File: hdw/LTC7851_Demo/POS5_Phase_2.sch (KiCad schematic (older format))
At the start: 0 parts

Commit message: Duplicated master phase, added status LEDs and a few test points
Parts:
- added C? (x2): 1uF, symbol Custom_Library:C_Custom
- added C? (x2): 0.1uF, symbol Custom_Library:C_Custom
- added C?: 0.22uF, symbol Custom_Library:C_Custom
- added C? (x2): 22uF, symbol Custom_Library:C_Custom
- added C? (x2): 100uF, symbol Custom_Library:C_Custom
- added C? (x6): 100uF, symbol Custom_Library:CP_Tant_Custom
- added L?: 0.47uH, symbol Custom_Library:L_Custom
- added R? (x2): 2, symbol Custom_Library:R_Custom
- added R?: 1.4k, symbol Custom_Library:R_Custom
- added TP? (x2): TP, symbol Custom_Library:TP
- added U?: SiC779, symbol Custom_Library:SiC779
- added U?: LTC7851UHH, symbol Custom_Library:LTC7851UHH
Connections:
- net labels added: +12V, +5.5V_MNG, +5V, GND, POS5_COMP, POS5_EXTVCC, POS5_IAVG, POS5_ILIM, POS5_ISNS1_+, POS5_ISNS1_-, POS5_PGOOD_OC, POS5_RUN, POS5_SMOD, POS5_SS, POS5_VOSNS, ~POS5_THDN
- wire segments 0 -> 110
- no-connect marks 0 -> 2
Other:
- note added: "Remove bulk caps from onsheet when bringing into project"
- note added: "Route as diff pair"

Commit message: Assigned some custom footprints
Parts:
- U?: footprint (none) -> Custom Footprints Library:MLP66-40_6x6mm_Pitch0.5mm
- U?: footprint (none) -> Custom Footprints Library:QFN-58-1EP_9x5mm_Pitch0.4mm
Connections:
- net labels added: POS5_ISNS2_+, POS5_ISNS2_-
- net labels removed: POS5_ISNS1_+, POS5_ISNS1_-
- wire segments 110 -> 112
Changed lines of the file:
@@
 F 0 "U?" H 6080 960 50  0000 C CNN
 F 1 "SiC779" H 6080 4660 50  0000 C CNN
-F 2 "" H 4430 3560 50  0001 C CNN
+F 2 "Custom Footprints Library:MLP66-40_6x6mm_Pitch0.5mm" H 4430 3560 50  0001 C CNN
 F 3 "http://www.vishay.com/docs/67538/sic779.pdf" H 6080 2810 50  0001 C CNN
 F 4 "SIC779CD-T1-GE3CT-ND" H 6080 2810 50  0001 C CNN "Digi-Key PN"
@@
 F 0 "U?" H 2910 2160 50  0000 R CNN
 F 1 "LTC7851UHH" H 2510 6260 50  0000 C CNN
-F 2 "" H -140 4910 50  0001 C CNN
+F 2 "Custom Footprints Library:QFN-58-1EP_9x5mm_Pitch0.4mm" H -140 4910 50  0001 C CNN
 F 3 "http://www.analog.com/media/en/technical-documentation/data-sheets/LTC7851.pdf" H 2510 4210 50  0001 C CNN
 F 4 "LTC7851IUHH#PBF-ND" H 2510 4210 50  0001 C CNN "Digi-Key PN"
@@
 POS5_RUN
 Text Label 3160 3310 0    50   ~ 0
-POS5_ISNS1_+
+POS5_ISNS2_+
 Text Label 3160 3410 0    50   ~ 0
-POS5_ISNS1_-
+POS5_ISNS2_-
 Text Notes 3270 3670 0    50   ~ 0
 Route as diff pair
@@
 Text GLabel 3060 5110 2    50   UnSpc ~ 0
 POS5_EXTVCC
+Wire Wire Line
+	6730 4110 6810 4110
+Wire Wire Line
+	6810 4110 6810 4010
+Connection ~ 6810 4010
 $EndSCHEMATC

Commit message: Annotated schematic
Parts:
- gave numbers to parts that had none: 23

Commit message: Added Digi-Key part numbers for all parts
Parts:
- C504, C509: Digi-Key PN PN -> 1276-6524-1-ND
- C506, C508: Digi-Key PN PN -> 490-4779-1-ND
- C510: Digi-Key PN PN -> 490-5402-1-ND
- C512: Digi-Key PN PN -> 587-3432-1-ND
- R501, R502: Digi-Key PN PN -> RMCF0603FT2R00CT-ND
- R503: Digi-Key PN PN -> P1.40KHCT-ND
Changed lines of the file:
@@
 F 5 "16V" H 4410 1340 50  0000 R CNN "Voltage"
 F 6 "X7R" H 4410 1240 50  0000 R CNN "Dielectric"
-F 7 "PN" H 4985 1840 60  0001 C CNN "Digi-Key PN"
+F 7 "1276-6524-1-ND" H 4985 1840 60  0001 C CNN "Digi-Key PN"
 	1    4560 1340
 	1    0    0    -1
@@
 F 2 "" H 6980 2470 50  0001 C CNN
 F 3 "" H 6980 2470 50  0001 C CNN
-F 4 "PN" H 7280 2870 60  0001 C CNN "Digi-Key PN"
+F 4 "RMCF0603FT2R00CT-ND" H 7280 2870 60  0001 C CNN "Digi-Key PN"
 F 5 "0603" H 7080 2550 50  0000 L CNN "display_footprint"
 F 6 "1%" H 7080 2470 50  0000 L CNN "Tolerance"
@@
 F 5 "50V" H 6830 2850 50  0000 R CNN "Voltage"
 F 6 "X7R" H 6830 2750 50  0000 R CNN "Dielectric"
-F 7 "PN" H 7405 3350 60  0001 C CNN "Digi-Key PN"
+F 7 "490-4779-1-ND" H 7405 3350 60  0001 C CNN "Digi-Key PN"
 	1    6980 2850
 	1    0    0    -1
@@
 F 2 "" H 7190 3770 50  0001 C CNN
 F 3 "" H 7190 3770 50  0001 C CNN
-F 4 "PN" H 7490 4170 60  0001 C CNN "Digi-Key PN"
+F 4 "P1.40KHCT-ND" H 7490 4170 60  0001 C CNN "Digi-Key PN"
 F 5 "0603" H 7290 3850 50  0000 L CNN "display_footprint"
 F 6 "1%" H 7290 3770 50  0000 L CNN "Tolerance"
@@
 F 2 "" H 7478 3890 50  0001 C CNN
 F 3 "" H 7465 4140 50  0001 C CNN
-F 4 "PN" H 7865 4540 60  0001 C CNN "Digi-Key PN"
+F 4 "490-5402-1-ND" H 7865 4540 60  0001 C CNN "Digi-Key PN"
 F 5 "0603" V 7098 4040 50  0000 C CNN "display_footprint"
 F 6 "50V" V 7189 4040 50  0000 C CNN "Voltage"
@@
 F 5 "10V" H 8270 3540 50  0000 R CNN "Voltage"
 F 6 "X5R" H 8270 3440 50  0000 R CNN "Dielectric"
-F 7 "PN" H 8845 4040 60  0001 C CNN "Digi-Key PN"
+F 7 "587-3432-1-ND" H 8845 4040 60  0001 C CNN "Digi-Key PN"
 	1    8420 3540
 	1    0    0    -1
@@
 F 5 "50V" H 5030 1870 50  0000 R CNN "Voltage"
 F 6 "X7R" H 5030 1770 50  0000 R CNN "Dielectric"
-F 7 "PN" H 5605 2370 60  0001 C CNN "Digi-Key PN"
+F 7 "490-4779-1-ND" H 5605 2370 60  0001 C CNN "Digi-Key PN"
 	1    5180 1870
 	1    0    0    -1
@@
 F 2 "" H 5180 1340 50  0001 C CNN
 F 3 "" H 5180 1340 50  0001 C CNN
-F 4 "PN" H 5480 1740 60  0001 C CNN "Digi-Key PN"
+F 4 "RMCF0603FT2R00CT-ND" H 5480 1740 60  0001 C CNN "Digi-Key PN"
 F 5 "0603" H 5280 1420 50  0000 L CNN "display_footprint"
 F 6 "1%" H 5280 1340 50  0000 L CNN "Tolerance"
@@
 F 5 "16V" H 7130 1340 50  0000 R CNN "Voltage"
 F 6 "X7R" H 7130 1240 50  0000 R CNN "Dielectric"
-F 7 "PN" H 7705 1840 60  0001 C CNN "Digi-Key PN"
+F 7 "1276-6524-1-ND" H 7705 1840 60  0001 C CNN "Digi-Key PN"
 	1    7280 1340
 	1    0    0    -1

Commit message: Assigned footprints
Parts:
- C501, C502, C503, C505, C507, C515: footprint (none) -> Capacitors_Tantalum_SMD:CP_Tantalum_Case-B_EIA-3528-21_Reflow
- C504: footprint (none) -> Capacitors_SMD:C_0603_HandSoldering
- C506, C508, C509, C510: footprint (none) -> Capacitors_SMD:C_0603
- C511, C512, C513, C514: footprint (none) -> Capacitors_SMD:C_1210
- L501: footprint (none) -> Inductors_SMD:L_Vishay_IHLP-4040
- R501, R502, R503: footprint (none) -> Resistors_SMD:R_0603
- TP501, TP502: footprint (none) -> Measurement_Points:Measurement_Point_Round-SMD-Pad_Small
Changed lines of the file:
@@
 F 0 "C504" H 4585 1440 50  0000 L CNN
 F 1 "1uF" H 4585 1240 50  0000 L CNN
-F 2 "" H 4598 1190 50  0001 C CNN
+F 2 "Capacitors_SMD:C_0603_HandSoldering" H 4598 1190 50  0001 C CNN
 F 3 "" H 4585 1440 50  0001 C CNN
 F 4 "0603" H 4410 1440 50  0000 R CNN "display_footprint"
@@
 F 0 "TP501" V 5430 2960 50  0000 L CNN
 F 1 "TP" H 5430 2960 50  0001 C CNN
-F 2 "" H 5430 2810 60  0000 C CNN
+F 2 "Measurement_Points:Measurement_Point_Round-SMD-Pad_Small" H 5430 2810 60  0001 C CNN
 F 3 "" H 5430 2810 60  0000 C CNN
 	1    5430 2810
@@
 F 0 "TP502" V 5430 3060 50  0000 L CNN
 F 1 "TP" H 5430 3060 50  0001 C CNN
-F 2 "" H 5430 2910 60  0000 C CNN
+F 2 "Measurement_Points:Measurement_Point_Round-SMD-Pad_Small" H 5430 2910 60  0001 C CNN
 F 3 "" H 5430 2910 60  0000 C CNN
 	1    5430 2910
@@
 F 0 "L501" V 7390 3310 50  0000 C CNN
 F 1 "0.47uH" V 7515 3310 50  0000 C CNN
-F 2 "" H 7440 3310 50  0001 C CNN
+F 2 "Inductors_SMD:L_Vishay_IHLP-4040" H 7440 3310 50  0001 C CNN
 F 3 "" H 7440 3310 50  0001 C CNN
 F 4 "541-2595-1-ND" H 7440 3310 50  0001 C CNN "Digi-Key PN"
@@
 F 0 "R502" H 6880 2470 50  0000 R CNN
 F 1 "2" V 6980 2470 50  0000 C CNN
-F 2 "" H 6980 2470 50  0001 C CNN
+F 2 "Resistors_SMD:R_0603" H 6980 2470 50  0001 C CNN
 F 3 "" H 6980 2470 50  0001 C CNN
 F 4 "RMCF0603FT2R00CT-ND" H 7280 2870 60  0001 C CNN "Digi-Key PN"
@@
 F 0 "C508" H 7005 2950 50  0000 L CNN
 F 1 "0.1uF" H 7005 2750 50  0000 L CNN
-F 2 "" H 7018 2700 50  0001 C CNN
+F 2 "Capacitors_SMD:C_0603" H 7018 2700 50  0001 C CNN
 F 3 "" H 7005 2950 50  0001 C CNN
 F 4 "0603" H 6830 2950 50  0000 R CNN "display_footprint"
@@
 F 0 "R503" H 7290 3920 50  0000 L CNN
 F 1 "1.4k" V 7190 3770 40  0000 C CNN
-F 2 "" H 7190 3770 50  0001 C CNN
+F 2 "Resistors_SMD:R_0603" H 7190 3770 50  0001 C CNN
 F 3 "" H 7190 3770 50  0001 C CNN
 F 4 "P1.40KHCT-ND" H 7490 4170 60  0001 C CNN "Digi-Key PN"
@@
 F 0 "C510" V 6916 4040 50  0000 C CNN
 F 1 "0.22uF" V 7007 3910 50  0000 L CNN
-F 2 "" H 7478 3890 50  0001 C CNN
+F 2 "Capacitors_SMD:C_0603" H 7478 3890 50  0001 C CNN
 F 3 "" H 7465 4140 50  0001 C CNN
 F 4 "490-5402-1-ND" H 7865 4540 60  0001 C CNN "Digi-Key PN"
@@
 F 0 "C511" H 7905 1440 50  0000 L CNN
 F 1 "22uF" H 7905 1240 50  0000 L CNN
-F 2 "" H 7918 1190 50  0001 C CNN
+F 2 "Capacitors_SMD:C_1210" H 7918 1190 50  0001 C CNN
 F 3 "" H 7905 1440 50  0001 C CNN
 F 4 "445-1436-1-ND" H 8305 1840 60  0001 C CNN "Digi-Key PN"
@@
 F 0 "C512" H 8445 3640 50  0000 L CNN
 F 1 "100uF" H 8445 3440 50  0000 L CNN
-F 2 "" H 8458 3390 50  0001 C CNN
+F 2 "Capacitors_SMD:C_1210" H 8458 3390 50  0001 C CNN
 F 3 "" H 8445 3640 50  0001 C CNN
 F 4 "1210" H 8270 3640 50  0000 R CNN "display_footprint"
@@
 F 0 "C506" H 5205 1970 50  0000 L CNN
 F 1 "0.1uF" H 5205 1770 50  0000 L CNN
-F 2 "" H 5218 1720 50  0001 C CNN
+F 2 "Capacitors_SMD:C_0603" H 5218 1720 50  0001 C CNN
 F 3 "" H 5205 1970 50  0001 C CNN
 F 4 "0603" H 5030 1970 50  0000 R CNN "display_footprint"
@@
 F 0 "R501" H 5080 1340 50  0000 R CNN
 F 1 "2" V 5180 1340 50  0000 C CNN
-F 2 "" H 5180 1340 50  0001 C CNN
+F 2 "Resistors_SMD:R_0603" H 5180 1340 50  0001 C CNN
 F 3 "" H 5180 1340 50  0001 C CNN
 F 4 "RMCF0603FT2R00CT-ND" H 5480 1740 60  0001 C CNN "Digi-Key PN"
@@
 F 0 "C509" H 7305 1440 50  0000 L CNN
 F 1 "1uF" H 7305 1240 50  0000 L CNN
-F 2 "" H 7318 1190 50  0001 C CNN
+F 2 "Capacitors_SMD:C_0603" H 7318 1190 50  0001 C CNN
 F 3 "" H 7305 1440 50  0001 C CNN
 F 4 "0603" H 7130 1440 50  0000 R CNN "display_footprint"
@@
 F 0 "C515" H 9645 3640 50  0000 L CNN
 F 1 "100uF" H 9645 3440 50  0000 L CNN
-F 2 "" H 9658 3390 50  0001 C CNN
+F 2 "Capacitors_Tantalum_SMD:CP_Tantalum_Case-B_EIA-3528-21_Reflow" H 9658 3390 50  0001 C CNN
 F 3 "" H 9645 3640 50  0001 C CNN
 F 4 "478-9994-1-ND" H 9620 3540 50  0001 C CNN "Digi-Key PN"
@@
 F 0 "C514" H 9045 3640 50  0000 L CNN
 F 1 "100uF" H 9045 3440 50  0000 L CNN
-F 2 "" H 9058 3390 50  0001 C CNN
+F 2 "Capacitors_SMD:C_1210" H 9058 3390 50  0001 C CNN
 F 3 "" H 9045 3640 50  0001 C CNN
 F 4 "587-3432-1-ND" H 9445 4040 60  0001 C CNN "Digi-Key PN"
@@
 F 0 "C513" H 8505 1440 50  0000 L CNN
 F 1 "22uF" H 8505 1240 50  0000 L CNN
-F 2 "" H 8518 1190 50  0001 C CNN
+F 2 "Capacitors_SMD:C_1210" H 8518 1190 50  0001 C CNN
 F 3 "" H 8505 1440 50  0001 C CNN
 F 4 "445-1436-1-ND" H 8905 1840 60  0001 C CNN "Digi-Key PN"
@@
 F 0 "C501" H 3355 7470 50  0000 L CNN
 F 1 "100uF" H 3355 7270 50  0000 L CNN
-F 2 "" H 3368 7220 50  0001 C CNN
+F 2 "Capacitors_Tantalum_SMD:CP_Tantalum_Case-B_EIA-3528-21_Reflow" H 3368 7220 50  0001 C CNN
 F 3 "" H 3355 7470 50  0001 C CNN
 F 4 "478-9994-1-ND" H 3330 7370 50  0001 C CNN "Digi-Key PN"
@@
 F 0 "C502" H 3955 7470 50  0000 L CNN
 F 1 "100uF" H 3955 7270 50  0000 L CNN
-F 2 "" H 3968 7220 50  0001 C CNN
+F 2 "Capacitors_Tantalum_SMD:CP_Tantalum_Case-B_EIA-3528-21_Reflow" H 3968 7220 50  0001 C CNN
 F 3 "" H 3955 7470 50  0001 C CNN
 F 4 "478-9994-1-ND" H 3930 7370 50  0001 C CNN "Digi-Key PN"
@@
 F 0 "C503" H 4555 7470 50  0000 L CNN
 F 1 "100uF" H 4555 7270 50  0000 L CNN
-F 2 "" H 4568 7220 50  0001 C CNN
+F 2 "Capacitors_Tantalum_SMD:CP_Tantalum_Case-B_EIA-3528-21_Reflow" H 4568 7220 50  0001 C CNN
 F 3 "" H 4555 7470 50  0001 C CNN
 F 4 "478-9994-1-ND" H 4530 7370 50  0001 C CNN "Digi-Key PN"
@@
 F 0 "C505" H 5155 7470 50  0000 L CNN
 F 1 "100uF" H 5155 7270 50  0000 L CNN
-F 2 "" H 5168 7220 50  0001 C CNN
+F 2 "Capacitors_Tantalum_SMD:CP_Tantalum_Case-B_EIA-3528-21_Reflow" H 5168 7220 50  0001 C CNN
 F 3 "" H 5155 7470 50  0001 C CNN
 F 4 "478-9994-1-ND" H 5130 7370 50  0001 C CNN "Digi-Key PN"
@@
 F 0 "C507" H 5755 7470 50  0000 L CNN
 F 1 "100uF" H 5755 7270 50  0000 L CNN
-F 2 "" H 5768 7220 50  0001 C CNN
+F 2 "Capacitors_Tantalum_SMD:CP_Tantalum_Case-B_EIA-3528-21_Reflow" H 5768 7220 50  0001 C CNN
 F 3 "" H 5755 7470 50  0001 C CNN
 F 4 "478-9994-1-ND" H 5730 7370 50  0001 C CNN "Digi-Key PN"

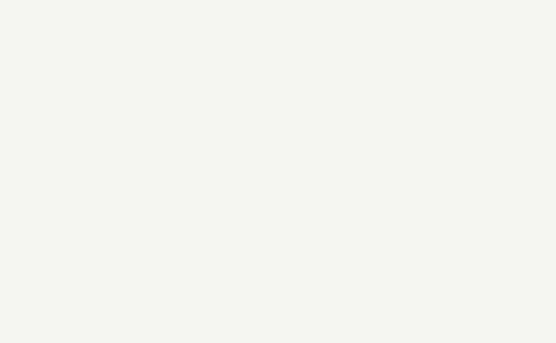
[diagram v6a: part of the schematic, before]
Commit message: Added page titles
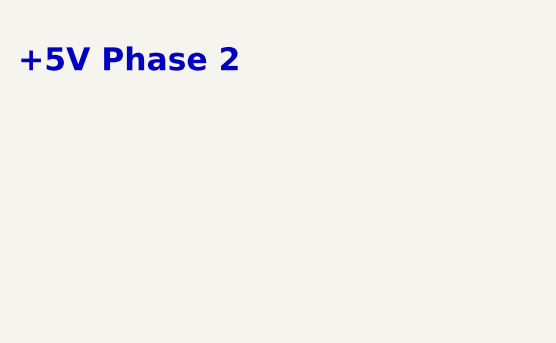
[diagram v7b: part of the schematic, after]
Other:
- note added: "+5V Phase 2"
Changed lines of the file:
@@
 	6810 4110 6810 4010
 Connection ~ 6810 4010
+Text Notes 540  690  0    100  ~ 20
++5V Phase 2
 $EndSCHEMATC

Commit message: More routing, removed GL ang GH phase test points
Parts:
- removed TP501, TP502: TP, Measurement_Points:Measurement_Point_Round-SMD-Pad_Small, symbol Custom_Library:TP
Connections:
- no-connect marks 2 -> 4
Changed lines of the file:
@@
 ~POS5_THDN
-$Comp
-L Custom_Library:TP TP?
-U 1 1 5BD16C37
-P 5430 2810
-AR Path="/5BB86F29/5BD16C37" Ref="TP?"  Part="1"
-AR Path="/5BB86F2C/5BD16C37" Ref="TP501"  Part="1"
-F 0 "TP501" V 5430 2960 50  0000 L CNN
-F 1 "TP" H 5430 2960 50  0001 C CNN
-F 2 "Measurement_Points:Measurement_Point_Round-SMD-Pad_Small" H 5430 2810 60  0001 C CNN
-F 3 "" H 5430 2810 60  0000 C CNN
-	1    5430 2810
-	0    -1   -1   0
-$EndComp
-$Comp
-L Custom_Library:TP TP?
-U 1 1 5BD16C3E
-P 5430 2910
-AR Path="/5BB86F29/5BD16C3E" Ref="TP?"  Part="1"
-AR Path="/5BB86F2C/5BD16C3E" Ref="TP502"  Part="1"
-F 0 "TP502" V 5430 3060 50  0000 L CNN
-F 1 "TP" H 5430 3060 50  0001 C CNN
-F 2 "Measurement_Points:Measurement_Point_Round-SMD-Pad_Small" H 5430 2910 60  0001 C CNN
-F 3 "" H 5430 2910 60  0000 C CNN
-	1    5430 2910
-	0    -1   -1   0
-$EndComp
 $Comp
 L power:GND #PWR?
@@
 Text Notes 540  690  0    100  ~ 20
 +5V Phase 2
+NoConn ~ 5430 2810
+NoConn ~ 5430 2910
 $EndSCHEMATC
